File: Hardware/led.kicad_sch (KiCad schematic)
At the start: 23 parts, among them U5 TLC59208FIPWR

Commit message: Version 0.1
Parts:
- C18: footprint Capacitor_SMD:C_0805_2012Metric_Pad1.18x1.45mm_HandSolder -> Capacitor_SMD:C_0603_1608Metric_Pad1.08x0.95mm_HandSolder
- R21, R22, R23, R24, R25, R26, R27, R28, R29, R30, R31, R32: footprint Resistor_SMD:R_0805_2012Metric_Pad1.20x1.40mm_HandSolder -> Resistor_SMD:R_0603_1608Metric_Pad0.98x0.95mm_HandSolder
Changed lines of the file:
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@@
     (property "Reference" "R23" (id 0) (at 102.235 97.79 90))
     (property "Value" "0" (id 1) (at 108.585 97.79 90))
-    (property "Footprint" "Resistor_SMD:R_0805_2012Metric_Pad1.20x1.40mm_HandSolder" (id 2) (at 105.41 97.028 90)
+    (property "Footprint" "Resistor_SMD:R_0603_1608Metric_Pad0.98x0.95mm_HandSolder" (id 2) (at 105.41 97.028 90)
       (effects (font (size 1.27 1.27)) hide)
     )
@@
     (property "Reference" "R32" (id 0) (at 185.42 127.635 90))
     (property "Value" "82" (id 1) (at 189.865 127.635 90))
-    (property "Footprint" "Resistor_SMD:R_0805_2012Metric_Pad1.20x1.40mm_HandSolder" (id 2) (at 187.325 132.588 90)
+    (property "Footprint" "Resistor_SMD:R_0603_1608Metric_Pad0.98x0.95mm_HandSolder" (id 2) (at 187.325 132.588 90)
       (effects (font (size 1.27 1.27)) hide)
     )
@@
     (property "Reference" "R26" (id 0) (at 185.42 62.865 90))
     (property "Value" "62" (id 1) (at 189.865 62.865 90))
-    (property "Footprint" "Resistor_SMD:R_0805_2012Metric_Pad1.20x1.40mm_HandSolder" (id 2) (at 187.325 67.818 90)
+    (property "Footprint" "Resistor_SMD:R_0603_1608Metric_Pad0.98x0.95mm_HandSolder" (id 2) (at 187.325 67.818 90)
       (effects (font (size 1.27 1.27)) hide)
     )
@@
     (property "Reference" "R21" (id 0) (at 101.6 107.95 90))
     (property "Value" "0" (id 1) (at 107.315 107.95 90))
-    (property "Footprint" "Resistor_SMD:R_0805_2012Metric_Pad1.20x1.40mm_HandSolder" (id 2) (at 104.14 112.268 90)
+    (property "Footprint" "Resistor_SMD:R_0603_1608Metric_Pad0.98x0.95mm_HandSolder" (id 2) (at 104.14 112.268 90)
       (effects (font (size 1.27 1.27)) hide)
     )
@@
       (effects (font (size 1.27 1.27)) (justify right))
     )
-    (property "Footprint" "Resistor_SMD:R_0805_2012Metric_Pad1.20x1.40mm_HandSolder" (id 2) (at 117.983 102.87 90)
+    (property "Footprint" "Resistor_SMD:R_0603_1608Metric_Pad0.98x0.95mm_HandSolder" (id 2) (at 117.983 102.87 90)
       (effects (font (size 1.27 1.27)) hide)
     )
@@
       (effects (font (size 1.27 1.27)) (justify left))
     )
-    (property "Footprint" "Capacitor_SMD:C_0805_2012Metric_Pad1.18x1.45mm_HandSolder" (id 2) (at 124.1552 128.27 0)
+    (property "Footprint" "Capacitor_SMD:C_0603_1608Metric_Pad1.08x0.95mm_HandSolder" (id 2) (at 124.1552 128.27 0)
       (effects (font (size 1.27 1.27)) hide)
     )
@@
     (property "Reference" "R22" (id 0) (at 102.235 90.17 90))
     (property "Value" "0" (id 1) (at 108.585 90.17 90))
-    (property "Footprint" "Resistor_SMD:R_0805_2012Metric_Pad1.20x1.40mm_HandSolder" (id 2) (at 105.41 94.488 90)
+    (property "Footprint" "Resistor_SMD:R_0603_1608Metric_Pad0.98x0.95mm_HandSolder" (id 2) (at 105.41 94.488 90)
       (effects (font (size 1.27 1.27)) hide)
     )
@@
     (property "Reference" "R25" (id 0) (at 185.42 51.435 90))
     (property "Value" "56" (id 1) (at 189.865 51.435 90))
-    (property "Footprint" "Resistor_SMD:R_0805_2012Metric_Pad1.20x1.40mm_HandSolder" (id 2) (at 187.325 56.388 90)
+    (property "Footprint" "Resistor_SMD:R_0603_1608Metric_Pad0.98x0.95mm_HandSolder" (id 2) (at 187.325 56.388 90)
       (effects (font (size 1.27 1.27)) hide)
     )
@@
     (property "Reference" "R30" (id 0) (at 185.42 107.315 90))
     (property "Value" "75" (id 1) (at 189.865 107.315 90))
-    (property "Footprint" "Resistor_SMD:R_0805_2012Metric_Pad1.20x1.40mm_HandSolder" (id 2) (at 187.325 112.268 90)
+    (property "Footprint" "Resistor_SMD:R_0603_1608Metric_Pad0.98x0.95mm_HandSolder" (id 2) (at 187.325 112.268 90)
       (effects (font (size 1.27 1.27)) hide)
     )
@@
     (property "Reference" "R29" (id 0) (at 185.42 97.155 90))
     (property "Value" "75" (id 1) (at 189.865 97.155 90))
-    (property "Footprint" "Resistor_SMD:R_0805_2012Metric_Pad1.20x1.40mm_HandSolder" (id 2) (at 187.325 102.108 90)
+    (property "Footprint" "Resistor_SMD:R_0603_1608Metric_Pad0.98x0.95mm_HandSolder" (id 2) (at 187.325 102.108 90)
       (effects (font (size 1.27 1.27)) hide)
     )
@@
     (property "Reference" "R31" (id 0) (at 185.42 117.475 90))
     (property "Value" "75" (id 1) (at 189.865 117.475 90))
-    (property "Footprint" "Resistor_SMD:R_0805_2012Metric_Pad1.20x1.40mm_HandSolder" (id 2) (at 187.325 122.428 90)
+    (property "Footprint" "Resistor_SMD:R_0603_1608Metric_Pad0.98x0.95mm_HandSolder" (id 2) (at 187.325 122.428 90)
       (effects (font (size 1.27 1.27)) hide)
     )
@@
     (property "Reference" "R27" (id 0) (at 185.42 74.295 90))
     (property "Value" "70" (id 1) (at 189.865 74.295 90))
-    (property "Footprint" "Resistor_SMD:R_0805_2012Metric_Pad1.20x1.40mm_HandSolder" (id 2) (at 187.325 79.248 90)
+    (property "Footprint" "Resistor_SMD:R_0603_1608Metric_Pad0.98x0.95mm_HandSolder" (id 2) (at 187.325 79.248 90)
       (effects (font (size 1.27 1.27)) hide)
     )
@@
     (property "Reference" "R28" (id 0) (at 185.42 85.725 90))
     (property "Value" "75" (id 1) (at 189.865 85.725 90))
-    (property "Footprint" "Resistor_SMD:R_0805_2012Metric_Pad1.20x1.40mm_HandSolder" (id 2) (at 187.325 90.678 90)
-      (effects (font (size 1.27 1.27)) hide)
-    )
+    (property "Footprint" "Resistor_SMD:R_0603_1608Metric_Pad0.98x0.95mm_HandSolder" (id 2) (at 187.325 90.678 90)
+      (effects (font (size 1.27 1.27)) hide)
+    )

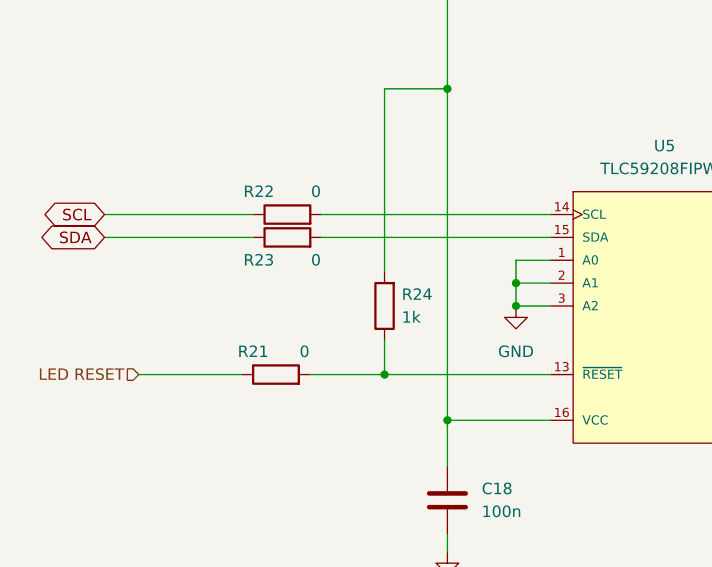
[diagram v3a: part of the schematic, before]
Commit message: Version 0.6 - 4 layer version
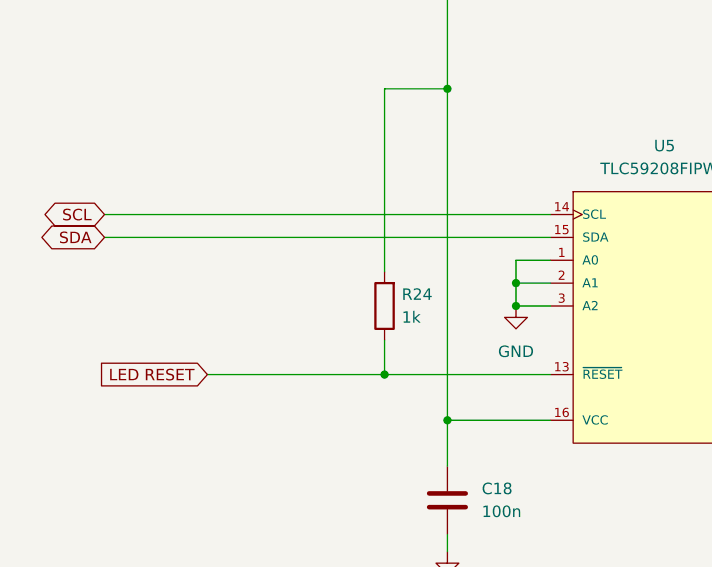
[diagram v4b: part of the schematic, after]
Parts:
- removed R21, R22, R23: 0, Resistor_SMD:R_0603_1608Metric_Pad0.98x0.95mm_HandSolder, symbol Device:R
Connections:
- net LED RESET: now also R24.1, U5.13 (~{RESET})
- net SCL: now also U5.14 (SCL)
- net SDA: now also U5.15 (SDA)
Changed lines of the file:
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@@
     (stroke (width 0) (type default) (color 0 0 0 0))
   )
-  (wire (pts (xy 109.22 95.25) (xy 134.62 95.25))
+  (wire (pts (xy 85.09 95.25) (xy 134.62 95.25))
     (stroke (width 0) (type default) (color 0 0 0 0))
   )
@@
     (stroke (width 0) (type default) (color 0 0 0 0))
   )
-  (wire (pts (xy 109.22 92.71) (xy 134.62 92.71))
+  (wire (pts (xy 85.09 92.71) (xy 134.62 92.71))
     (stroke (width 0) (type default) (color 0 0 0 0))
   )
@@
     (stroke (width 0) (type default) (color 0 0 0 0))
   )
-  (wire (pts (xy 107.95 110.49) (xy 116.205 110.49))
-    (stroke (width 0) (type default) (color 0 0 0 0))
-  )
-  (wire (pts (xy 85.09 95.25) (xy 101.6 95.25))
+  (wire (pts (xy 96.52 110.49) (xy 116.205 110.49))
     (stroke (width 0) (type default) (color 0 0 0 0))
   )
@@
     (stroke (width 0) (type default) (color 0 0 0 0))
   )
-  (wire (pts (xy 85.09 92.71) (xy 101.6 92.71))
-    (stroke (width 0) (type default) (color 0 0 0 0))
-  )
   (wire (pts (xy 160.02 100.33) (xy 173.99 100.33))
     (stroke (width 0) (type default) (color 0 0 0 0))
@@
   )
   (wire (pts (xy 130.81 97.79) (xy 130.81 100.33))
-    (stroke (width 0) (type default) (color 0 0 0 0))
-  )
-  (wire (pts (xy 88.9 110.49) (xy 100.33 110.49))
     (stroke (width 0) (type default) (color 0 0 0 0))
   )
@@
     )
   )
+  (global_label "LED RESET" (shape input) (at 96.52 110.49 180) (fields_autoplaced)
+    (effects (font (size 1.27 1.27)) (justify right))
+    (property "Intersheet References" "${INTERSHEET_REFS}" (id 0) (at 83.9469 110.4106 0)
+      (effects (font (size 1.27 1.27)) (justify right) hide)
+    )
+  )
   (global_label "SDA" (shape bidirectional) (at 85.09 95.25 180) (fields_autoplaced)
     (effects (font (size 1.27 1.27)) (justify right))
@@
       (effects (font (size 1.27 1.27)) (justify right) hide)
     )
-  )
-  (hierarchical_label "LED RESET" (shape input) (at 88.9 110.49 180)
-    (effects (font (size 1.27 1.27)) (justify right))
-  )
-  (symbol (lib_id "Device:R") (at 105.41 95.25 90) (unit 1)
-    (in_bom yes) (on_board yes)
-    (property "Reference" "R23" (id 0) (at 102.235 97.79 90))
-    (property "Value" "0" (id 1) (at 108.585 97.79 90))
-    (property "Footprint" "Resistor_SMD:R_0603_1608Metric_Pad0.98x0.95mm_HandSolder" (id 2) (at 105.41 97.028 90)
-      (effects (font (size 1.27 1.27)) hide)
-    )
-    (property "Datasheet" "~" (id 3) (at 105.41 95.25 0)
-      (effects (font (size 1.27 1.27)) hide)
-    )
-    (pin "1")
-    (pin "2")
   )
   (symbol (lib_id "Device:LED") (at 201.93 100.33 0) (unit 1)
@@
     (pin "1")
   )
-  (symbol (lib_id "Device:R") (at 104.14 110.49 90) (unit 1)
-    (in_bom yes) (on_board yes)
-    (property "Reference" "R21" (id 0) (at 101.6 107.95 90))
-    (property "Value" "0" (id 1) (at 107.315 107.95 90))
-    (property "Footprint" "Resistor_SMD:R_0603_1608Metric_Pad0.98x0.95mm_HandSolder" (id 2) (at 104.14 112.268 90)
-      (effects (font (size 1.27 1.27)) hide)
-    )
-    (property "Datasheet" "~" (id 3) (at 104.14 110.49 0)
-      (effects (font (size 1.27 1.27)) hide)
-    )
-    (pin "1")
-    (pin "2")
-  )
   (symbol (lib_id "Device:R") (at 116.205 102.87 180) (unit 1)
     (in_bom yes) (on_board yes) (fields_autoplaced)
@@
       (effects (font (size 1.27 1.27)) hide)
     )
-    (pin "1")
-    (pin "2")
-  )
-  (symbol (lib_id "Device:R") (at 105.41 92.71 90) (unit 1)
-    (in_bom yes) (on_board yes)
-    (property "Reference" "R22" (id 0) (at 102.235 90.17 90))
-    (property "Value" "0" (id 1) (at 108.585 90.17 90))
-    (property "Footprint" "Resistor_SMD:R_0603_1608Metric_Pad0.98x0.95mm_HandSolder" (id 2) (at 105.41 94.488 90)
-      (effects (font (size 1.27 1.27)) hide)
-    )
-    (property "Datasheet" "~" (id 3) (at 105.41 92.71 0)
-      (effects (font (size 1.27 1.27)) hide)
-    )
